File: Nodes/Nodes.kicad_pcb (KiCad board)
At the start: 2 copper layers, 80.9 x 83.9 mm, 31 parts, among them J1 Conn_01x04_Socket, J2 Barrel_Jack_MountingPin, J3 Screw_Terminal_01x03, J4 Screw_Terminal_01x03, SW1 SW_Push, U1 NRF24L01_Breakout, U2 NRF24L01_Breakout, U3 AMS1117-3.3, U4 YAAJ_BluePill_Part_Like, U5 NRF24L01_Breakout

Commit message: chore: add labels to switch
rename OLED port on pcb to I2C, added "TRAIN DIR" text to switch on schematic and PCB.
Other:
- board text added: "I2C"
- board text added: "TRAIN DIR"
- board text removed: "OLED"
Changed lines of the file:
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@@
 		(fp_arc
 			(start 3.834188 38.743851)
-			(mid 3.811617 38.645123)
+			(mid 3.811619 38.645125)
 			(end 3.8118 38.543851)
 			(stroke
@@
 	)
 	(gr_text "SIGNAL RST"
-		(at 122.4 61.625 90)
+		(at 122.5 61.5 90)
 		(layer "F.SilkS" knockout)
 		(effects
@@
 		)
 	)
+	(gr_text "TRAIN DIR"
+		(at 130.5 61 90)
+		(layer "F.SilkS" knockout)
+		(effects
+			(font
+				(size 1 1)
+				(thickness 0.2)
+				(bold yes)
+			)
+			(justify left bottom)
+		)
+	)
 	(gr_text "NRF2"
 		(at 166.2 105 0)
@@
 		)
 	)
-	(gr_text "OLED"
+	(gr_text "I2C"
 		(at 128.5 130 180)
 		(layer "F.SilkS" knockout)

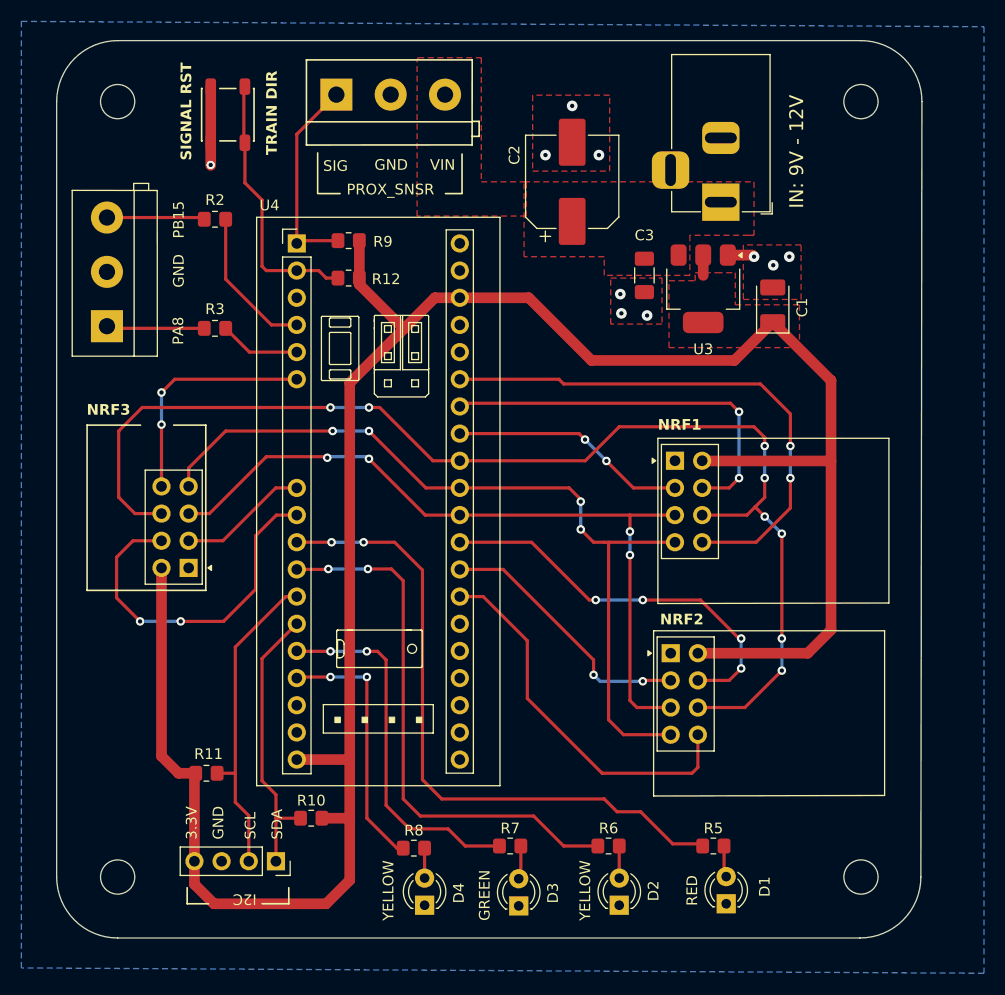
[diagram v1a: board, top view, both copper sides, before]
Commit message: chore: change connections for NRF24(U5), IO port and LEDs
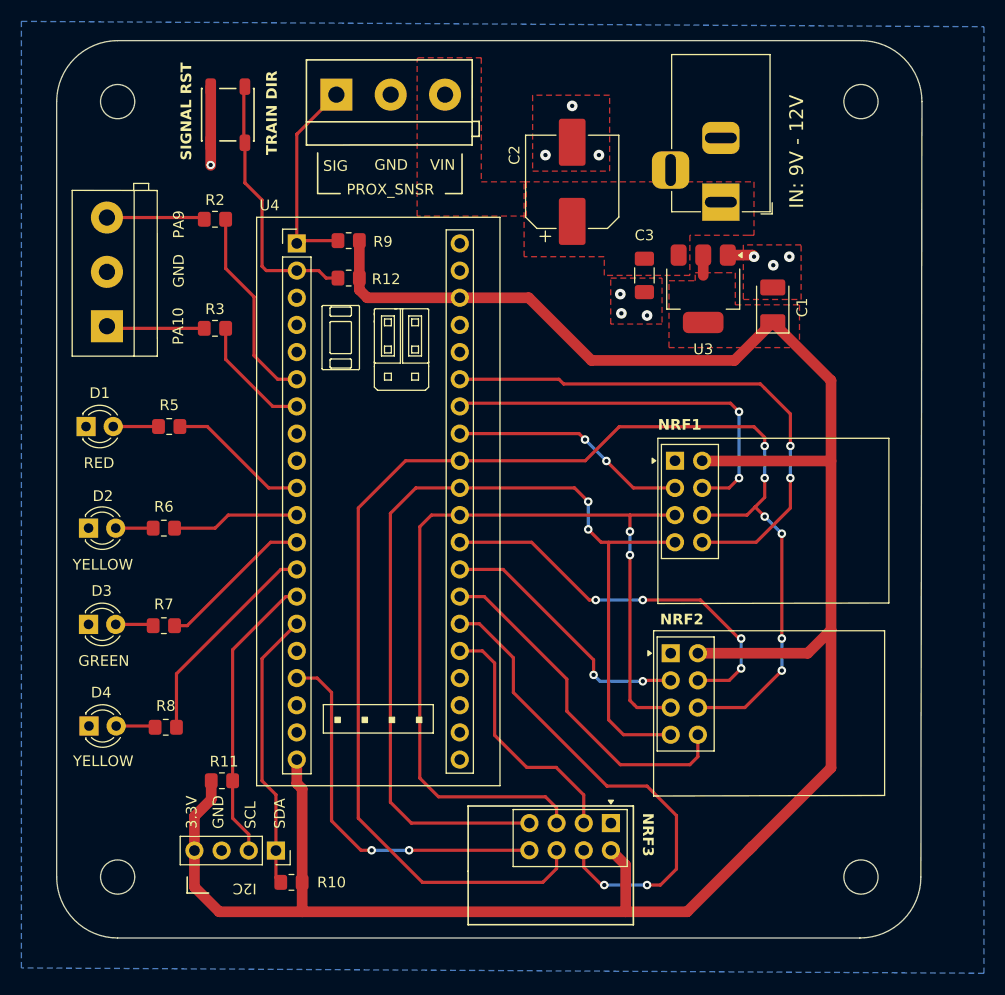
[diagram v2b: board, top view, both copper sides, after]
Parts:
- moved D1 74.7 mm to (112.5, 86.4), turned to 0 degrees
- moved R5 64.2 mm to (120.3, 86.4), turned to 180 degrees
- moved D2 60.9 mm to (112.8, 95.9), turned to 0 degrees
- moved R6 51.1 mm to (119.8, 95.9), turned to 180 degrees
- moved D3 48.1 mm to (112.8, 104.9), turned to 0 degrees
- moved U5 46.1 mm to (161.6, 123.5), turned to -90 degrees
- moved R7 38.4 mm to (119.8, 105.0), turned to 180 degrees
- moved D4 35.6 mm to (112.8, 114.4), turned to 0 degrees
- moved R8 25.8 mm to (120.0, 114.5), turned to 180 degrees
- moved R10 6.28 mm to (131.8, 129.0)
- moved R11 1.61 mm to (125.2, 119.5)
- moved J1 1.00 mm to (130.3, 126.0)
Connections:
- net /PA8 renamed /PA10
- net /PB15 renamed /PA9
- R2 pad 2: /PA15R -> /PA9R
- R3 pad 2: /PA8R -> /PA10R
- U4 pad 10: /NRF_CE3 -> /R_RED
- U4 pad 11: /NRF_CSN3 -> /R_YELLOW1
- U4 pad 12: /R_RED -> /R_GREEN
- U4 pad 13: /R_YELLOW1 -> /R_YELLOW2
- U4 pad 16: /R_GREEN -> unconnected-(U4-PB8-Pad16)
- U4 pad 17: /R_YELLOW2 -> /NRF_IRQ3
- U4 pad 25: unconnected-(U4-PA0-Pad25) -> /NRF_CE3
- U4 pad 26: unconnected-(U4-PA1-Pad26) -> /NRF_CSN3
- U4 pad 4: /PA15R -> unconnected-(U4-PB15-Pad4)
- U4 pad 5: /PA8R -> unconnected-(U4-PA8-Pad5)
- U4 pad 6: /NRF_IRQ3 -> /PA9R
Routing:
- net /R_RED: track 61.6 -> 13.3 mm, vias 2 -> 0
- net /R_YELLOW1: track 51.2 -> 11.9 mm, vias 2 -> 0
- net /R_GREEN: track 34.5 -> 14.7 mm, vias 2 -> 0
- net /PA9R: track 0.00 -> 19.0 mm
- net /NRF_MOSI: track 113.7 -> 131.6 mm, vias 8 -> 6
- net /NRF_MISO: track 77.6 -> 95.0 mm, vias 4 -> 2
- net /PA15R: track 14.3 -> 0.00 mm
- net /NRF_IRQ3: track 21.9 -> 35.4 mm
- net /NRF_SCK: track 71.4 -> 84.6 mm, vias 4 -> 2
- net /NRF_CSN3: track 33.4 -> 46.2 mm
- net /NRF_CE3: track 12.2 -> 23.8 mm
- net /PA10R: track 0.00 -> 11.4 mm
- net /PA8R: track 7.57 -> 0.00 mm
- net /R_YELLOW2: track 24.4 -> 20.3 mm, vias 2 -> 0
- net /NRF_IRQ2: track 35.5 -> 32.9 mm
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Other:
- board text added: "PA10"
- board text added: "PA9"
- board text removed: "PA8"
- board text removed: "PB15"

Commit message: fix: change silkscreen line width to 0.152 and update vendor link for resistors and NRF24
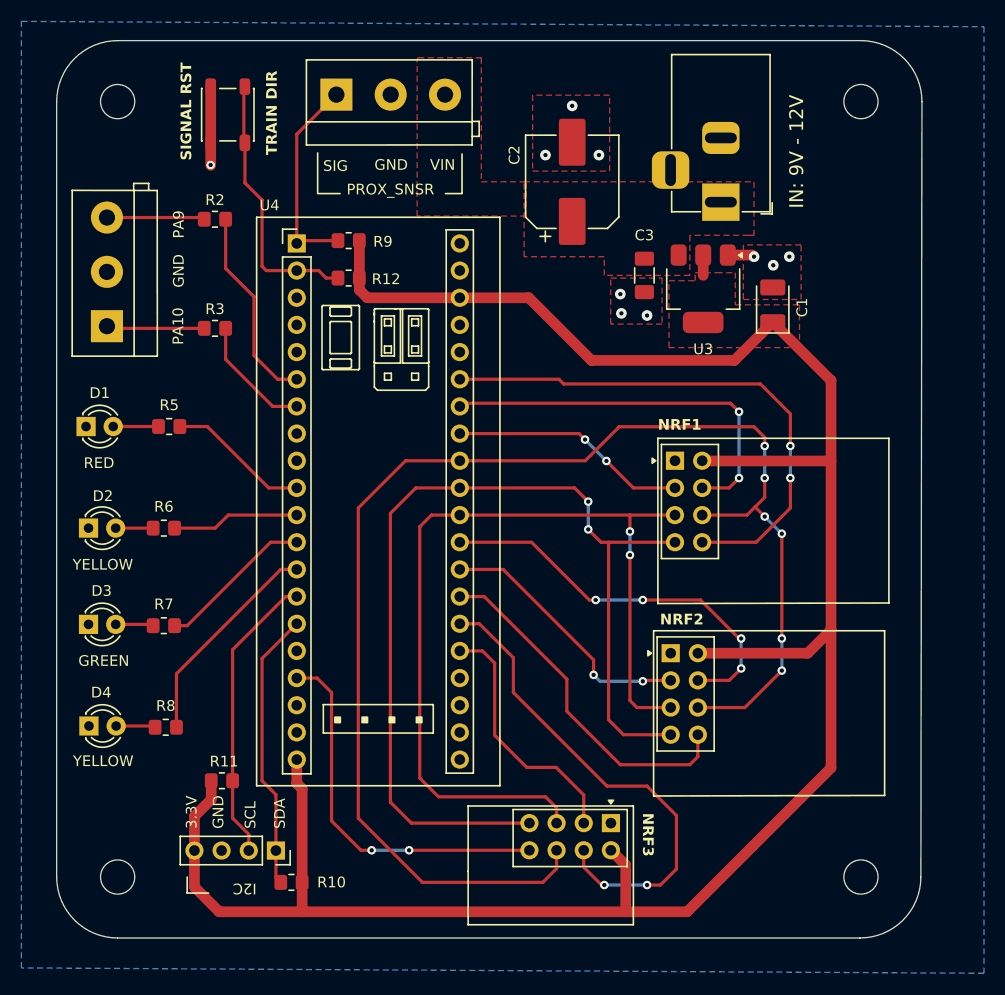
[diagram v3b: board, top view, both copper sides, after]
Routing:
- net +3.3V: track 216.6 -> 216.1 mm
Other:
- board text added: "OTAPS 1.1"
- board text removed: "OTAPS 1.0"

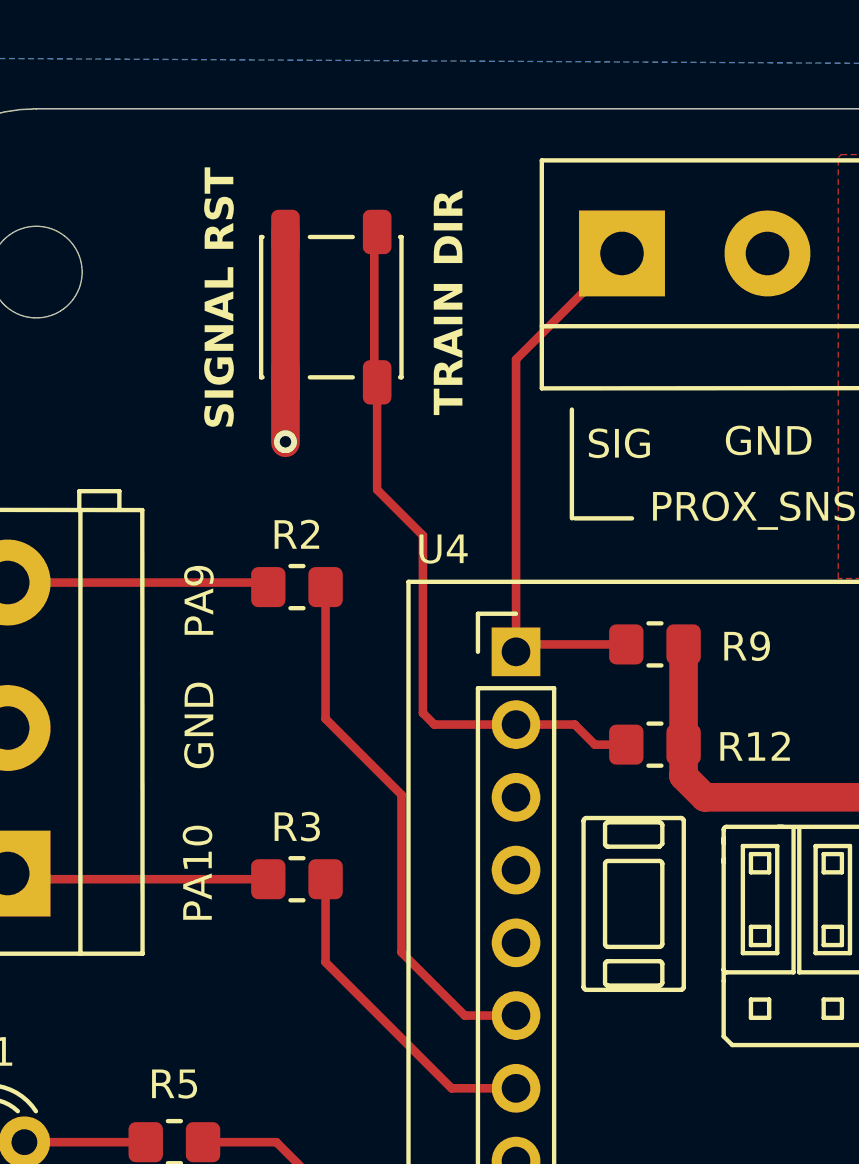
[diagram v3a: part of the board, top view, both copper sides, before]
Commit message: fix: change switch footprint changed the switch footprint and associated 3D model regenerated the gerbers
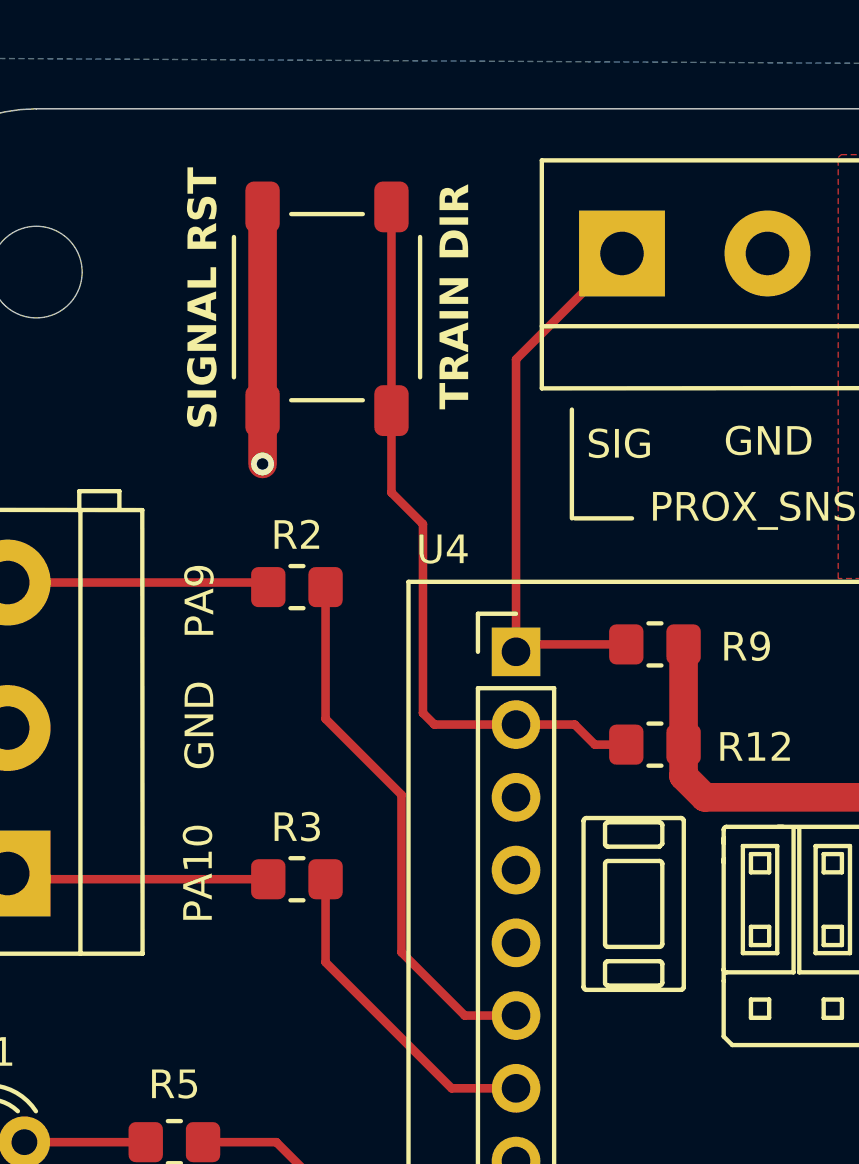
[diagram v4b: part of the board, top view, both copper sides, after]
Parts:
- moved SW1 0.40 mm to (125.4, 57.2)
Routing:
- net GND: track 9.92 -> 11.8 mm
- net /SGNL_RST_SWT: track 25.0 -> 25.7 mm
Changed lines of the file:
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@@
 		(fp_arc
 			(start 2.357533 5.902277)
-			(mid 2.386841 5.831583)
+			(mid 2.386841 5.831587)
 			(end 2.457533 5.802277)
 			(stroke
@@
 		(fp_arc
 			(start 3.107533 6.052277)
-			(mid 3.136826 5.981558)
+			(mid 3.136832 5.981593)
 			(end 3.207533 5.952277)
 			(stroke
@@
 		(fp_arc
 			(start 3.107533 7.402277)
-			(mid 3.136826 7.331558)
+			(mid 3.136832 7.331593)
 			(end 3.207533 7.302277)
 			(stroke
@@
 		(fp_arc
 			(start 3.107533 10.902277)
-			(mid 3.136826 10.831558)
+			(mid 3.136832 10.831593)
 			(end 3.207533 10.802277)
 			(stroke
@@
 		(fp_arc
 			(start 5.107533 10.202277)
-			(mid 5.078248 10.272979)
+			(mid 5.078254 10.273014)
 			(end 5.007533 10.302277)
 			(stroke
@@
 		(fp_arc
 			(start 5.107533 11.552277)
-			(mid 5.078248 11.622979)
+			(mid 5.078254 11.623014)
 			(end 5.007533 11.652277)
 			(stroke
@@
 		(fp_arc
 			(start 5.857533 11.702277)
-			(mid 5.828248 11.772979)
+			(mid 5.828254 11.773014)
 			(end 5.757533 11.802277)
 			(stroke
@@
 	(footprint "Button_Switch_SMD:SW_SPST_PTS647_Sx38"
 		(layer "F.Cu")
-		(at 125.8 57.225 90)
+		(at 125.4 57.225 90)
 		(descr "C&K Components SPST SMD PTS647 Series 4.5mm Tact Switch, 3.8mm Height, see https://www.ckswitches.com/media/2567/pts647.pdf")
 		(tags "SPST Button Switch")
@@
 		(attr smd)
 		(fp_line
-			(start 2.45 -2.45)
-			(end 2.45 -2.4)
+			(start -2.45 -3)
+			(end 2.45 -3)
 			(stroke
 				(width 0.152)
@@
 		)
 		(fp_line
-			(start -2.45 -2.45)
-			(end 2.45 -2.45)
+			(start 3.25 -1)
+			(end 3.25 1.5)
 			(stroke
 				(width 0.152)
@@
 		)
 		(fp_line
-			(start -2.45 -2.45)
-			(end -2.45 -2.4)
+			(start -3.25 -1)
+			(end -3.25 1.5)
 			(stroke
 				(width 0.152)
@@
 		)
 		(fp_line
-			(start 2.45 -0.75)
-			(end 2.45 0.75)
-			(stroke
-				(width 0.152)
-				(type solid)
-			)
-			(layer "F.SilkS")
-		)
-		(fp_line
-			(start -2.45 -0.75)
-			(end -2.45 0.75)
-			(stroke
-				(width 0.152)
-				(type solid)
-			)
-			(layer "F.SilkS")
-		)
-		(fp_line
-			(start 2.45 2.45)
-			(end 2.45 2.4)
-			(stroke
-				(width 0.152)
-				(type solid)
-			)
-			(layer "F.SilkS")
-		)
-		(fp_line
-			(start -2.45 2.45)
-			(end -2.45 2.4)
-			(stroke
-				(width 0.152)
-				(type solid)
-			)
-			(layer "F.SilkS")
-		)
-		(fp_line
-			(start -2.45 2.45)
-			(end 2.45 2.45)
+			(start -2.45 3.5)
+			(end 2.45 3.5)
 			(stroke
 				(width 0.152)
@@
 		)
 		(fp_rect
-			(start -3.65 -2.7)
-			(end 3.65 2.7)
+			(start -4.65 -3.25)
+			(end 4.75 3.75)
 			(stroke
 				(width 0.05)
@@
 		)
 		(fp_rect
-			(start -2.25 -2.25)
-			(end 2.25 2.25)
+			(start -3 -2.75)
+			(end 3 3.25)
 			(stroke
 				(width 0.1)
@@
 		(fp_circle
 			(center 0 0)
-			(end 1.15 0)
+			(end 1.25 0)
 			(stroke
 				(width 0.1)
@@
 		)
 		(pad "1" smd roundrect
-			(at -2.625 -1.6 90)
-			(size 1.55 1)
+			(at -3.6125 -2 90)
+			(size 1.775 1.2)
 			(layers "F.Cu" "F.Paste" "F.Mask")
 			(roundrect_rratio 0.25)
@@
 		)
 		(pad "1" smd roundrect
-			(at 2.625 -1.6 90)
-			(size 1.55 1)
+			(at 3.5 -2 90)
+			(size 1.775 1.2)
 			(layers "F.Cu" "F.Paste" "F.Mask")
 			(roundrect_rratio 0.25)
@@
 		)
 		(pad "2" smd roundrect
-			(at -2.625 1.6 90)
-			(size 1.55 1)
+			(at -3.6125 2.5 90)
+			(size 1.775 1.2)
 			(layers "F.Cu" "F.Paste" "F.Mask")
 			(roundrect_rratio 0.25)
@@
 		)
 		(pad "2" smd roundrect
-			(at 2.625 1.6 90)
-			(size 1.55 1)
+			(at 3.5 2.5 90)
+			(size 1.775 1.2)
 			(layers "F.Cu" "F.Paste" "F.Mask")
 			(roundrect_rratio 0.25)
@@
 			(pintype "passive")
 		)
-		(model "${KICAD8_3DMODEL_DIR}/Button_Switch_SMD.3dshapes/SW_SPST_PTS647Sx38.wrl"
+		(model "${KIPRJMOD}/3D_Models/button_smd_6x6x4.3.stp"
 			(offset
-				(xyz 0 0 0)
+				(xyz 0 -0.25 0)
 			)
 			(scale
@@
 			)
 			(rotate
-				(xyz 0 0 0)
+				(xyz 0 0 90)
 			)
 		)
@@
 	)
 	(gr_text "SIGNAL RST"
-		(at 122.5 61.5 90)
+		(at 121.9 61.5 90)
 		(layer "F.SilkS" knockout)
 		(effects
@@
 	)
 	(gr_text "TRAIN DIR"
-		(at 130.5 61 90)
+		(at 130.7 60.8 90)
 		(layer "F.SilkS" knockout)
 		(effects
@@
 	)
 	(segment
-		(start 124.2 61.9625)
-		(end 124.2 60.0875)
-		(width 1)
-		(layer "F.Cu")
-		(net 1)
-	)
-	(segment
-		(start 124.2 59.85)
-		(end 124.2 54.6)
+		(start 123.4 62.7)
+		(end 123.4 60.8375)
 		(width 1)
 		(layer "F.Cu")
@@
 	)
 	(segment
+		(start 123.4 60.8375)
+		(end 123.4 53.725)
+		(width 1)
+		(layer "F.Cu")
+		(net 1)
+	)
+	(segment
 		(start 172.55 70.35)
 		(end 174.85 70.35)
@@
 	)
 	(via
-		(at 124.2 61.925)
+		(at 123.4 62.7)
 		(size 0.8)
 		(drill 0.4)
@@
 	)
 	(segment
-		(start 129.4 71.8)
-		(end 129 71.4)
+		(start 127.9 60.8375)
+		(end 127.9 53.725)
 		(width 0.3)
 		(layer "F.Cu")
@@
 	)
 	(segment
-		(start 127.4 63.6)
-		(end 127.4 59.85)
+		(start 129 64.8)
+		(end 127.9 63.7)
 		(width 0.3)
 		(layer "F.Cu")
@@
 	)
 	(segment
-		(start 136.1 72.5)
-		(end 135 72.5)
+		(start 129 71.4)
+		(end 129 64.8)
 		(width 0.3)
 		(layer "F.Cu")
@@
 	)
 	(segment
-		(start 132.25 71.8)
-		(end 129.4 71.8)
+		(start 136.1 72.5)
+		(end 135 72.5)
 		(width 0.3)
 		(layer "F.Cu")
@@
 	)
 	(segment
-		(start 129 65.2)
-		(end 127.4 63.6)
+		(start 129.4 71.8)
+		(end 129 71.4)
 		(width 0.3)
 		(layer "F.Cu")
@@
 	)
 	(segment
-		(start 127.3 54.6)
-		(end 127.3 59.85)
+		(start 127.9 63.7)
+		(end 127.9 60.8375)
 		(width 0.3)
 		(layer "F.Cu")
@@
 	)
 	(segment
-		(start 129 71.4)
-		(end 129 65.2)
+		(start 134.3 71.8)
+		(end 132.25 71.8)
 		(width 0.3)
 		(layer "F.Cu")
@@
 	)
 	(segment
-		(start 134.3 71.8)
-		(end 132.25 71.8)
+		(start 132.25 71.8)
+		(end 129.4 71.8)
 		(width 0.3)
 		(layer "F.Cu")
